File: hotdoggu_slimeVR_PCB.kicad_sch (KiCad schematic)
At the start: 8 parts, among them J1 Conn_01x04_Pin, J2 Conn_01x02_Pin, SW1 SW_SPDT_312, U2 module_mpu6050

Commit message: pattern, sym, footprint update
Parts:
- U1: footprint hotdoggu_slimeVR_PCB:Geekble_Mini_ESP32C3 -> hotdoggu_slimeVR_PCB:Geekble_Mini_ESP32C3_SMD; symbol hotdoggu_slimeVR_PCB:Geekble_Mini_ESP32C3 -> hotdoggu_slimeVR_PCB:Geekble_Mini_ESP32C3FH4_SMD
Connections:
- net +3V3: now also U1.11 (3V3); no longer U1.20 (3V3)
- net GND: now also J1.4 (Pin_4), U1.15 (GPIO7/D7), U1.9 (GND); no longer J1.1 (Pin_1), U1.14 (GND), U1.2 (GND)
- net SCL: now also J1.3 (Pin_3), U1.6 (GPIO5/A5); no longer J1.4 (Pin_4), U1.5 (D5)
- net SDA: now also J1.1 (Pin_1), U1.5 (GPIO4/A4); no longer J1.3 (Pin_3), U1.6 (D4)
- net VBAT_SW: now also U1.7 (VUSB); no longer U1.1 (VIN)
- net at R1.2, R2.1: now also U1.1 (GPIO0/A0); no longer U1.10 (D0)
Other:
- moved on the sheet: *1, J1, J2, R1, R2, SW1, U2

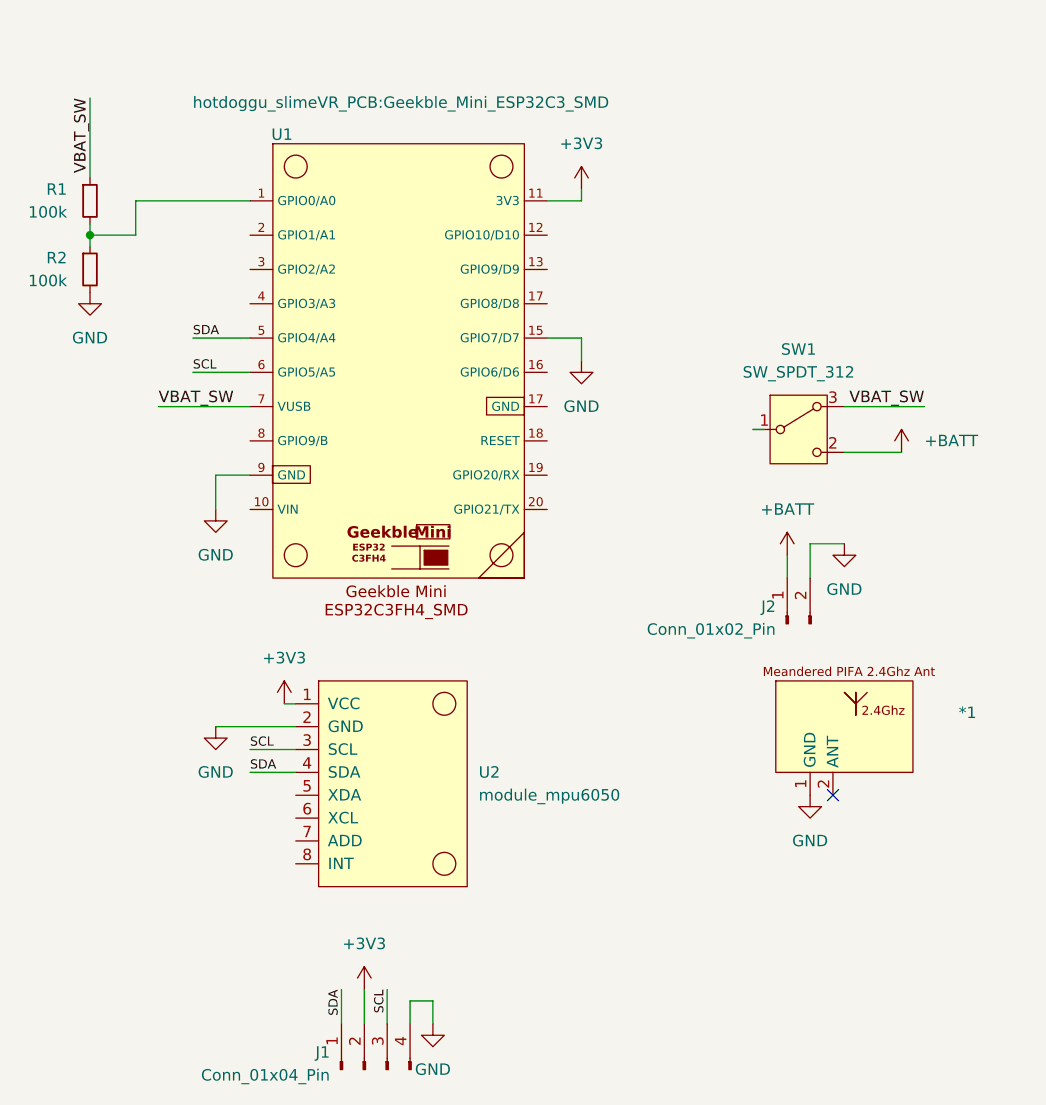
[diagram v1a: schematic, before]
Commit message: seperate sym, lib / update routing
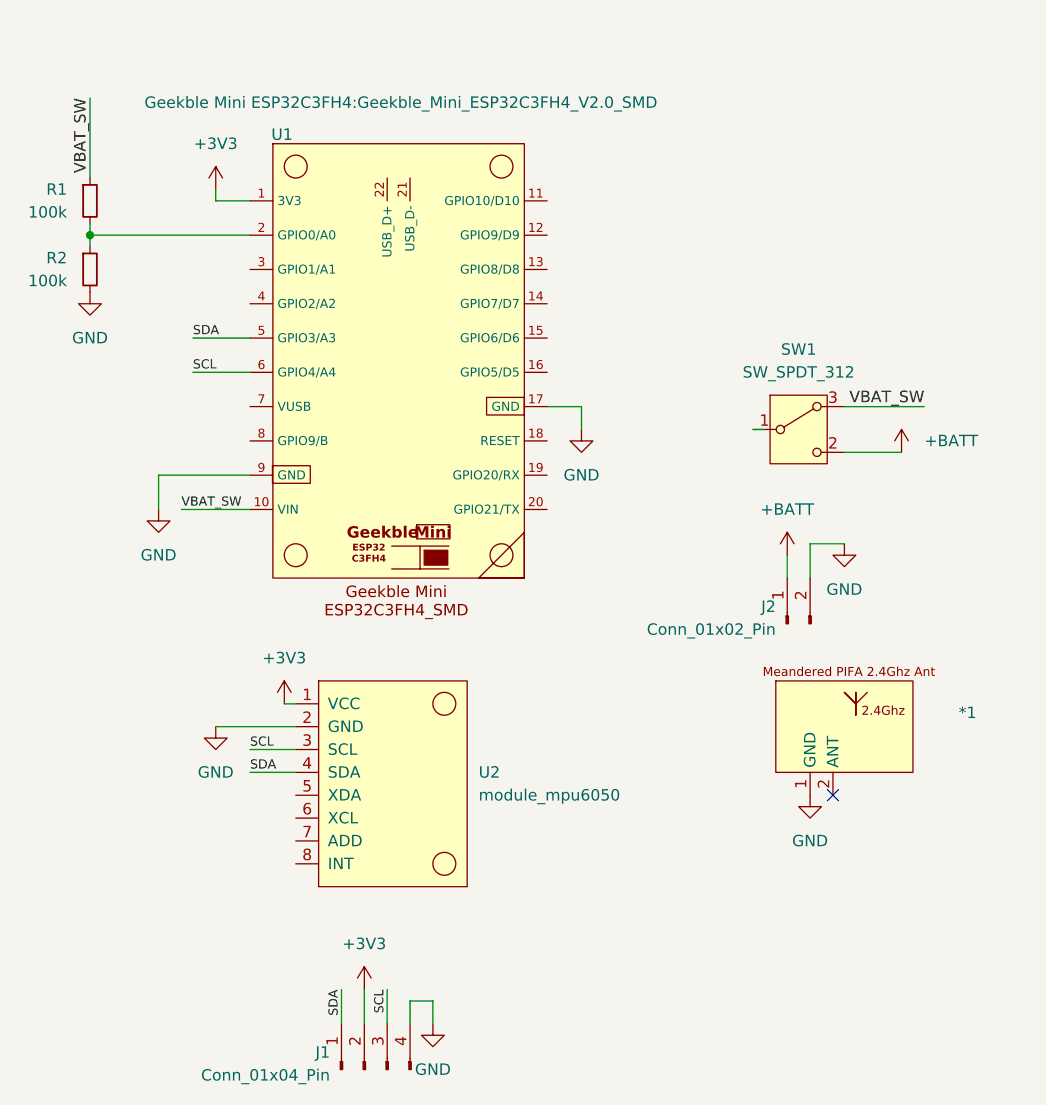
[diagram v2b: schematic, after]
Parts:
- U1: footprint hotdoggu_slimeVR_PCB:Geekble_Mini_ESP32C3_SMD -> Geekble Mini ESP32C3FH4:Geekble_Mini_ESP32C3FH4_V2.0_SMD; symbol hotdoggu_slimeVR_PCB:Geekble_Mini_ESP32C3FH4_SMD -> Geekble Mini ESP32C3FH4:Geekble_Mini_ESP32C3FH4_v2.0_SMD
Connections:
- net +3V3: now also U1.1 (3V3); no longer U1.11 (3V3)
- net GND: now also U1.17 (GND); no longer U1.15 (GPIO7/D7)
- net VBAT_SW: now also U1.10 (VIN); no longer U1.7 (VUSB)
- net at R1.2, R2.1: now also U1.2 (GPIO0/A0); no longer U1.1 (GPIO0/A0)

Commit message: changes for GeekbleMini V2.0
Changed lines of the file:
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@@
+	(wire
+		(pts
+			(xy 107.95 73.66) (xy 114.3 73.66)
+		)
+		(stroke
+			(width 0)
+			(type default)
+		)
+	)
 	(wire
 		(pts
@@
 		)
 	)
-	(wire
-		(pts
-			(xy 107.95 73.66) (xy 114.3 73.66)
-		)
-		(stroke
-			(width 0)
-			(type default)
+	(label "SCL"
+		(at 107.95 77.47 0)
+		(effects
+			(font
+				(size 1.016 1.016)
+			)
+			(justify left bottom)
 		)
 	)
@@
 		)
 	)
-	(label "SCL"
-		(at 107.95 77.47 0)
-		(effects
-			(font
-				(size 1.016 1.016)
-			)
-			(justify left bottom)
-		)
-	)
